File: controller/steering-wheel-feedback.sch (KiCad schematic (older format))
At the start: 5 parts

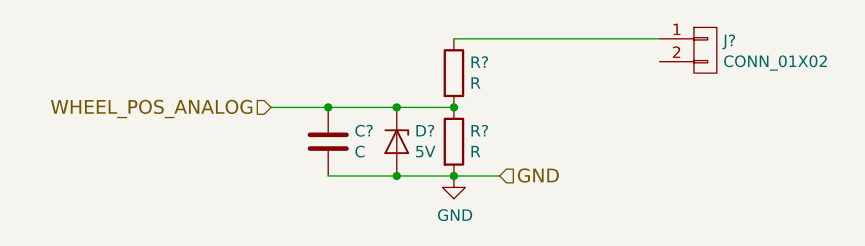
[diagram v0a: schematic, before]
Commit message: Add more stuff to controller, start sourcing parts
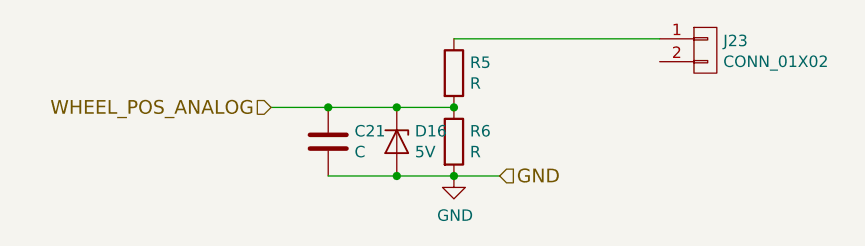
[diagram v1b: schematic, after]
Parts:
- gave numbers to parts that had none: 5
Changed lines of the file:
@@
 LIBS:mic-parts
 LIBS:controller-cache
-LIBS:line-interface-cache
 EELAYER 26 0
 EELAYER END
 $Descr A4 11693 8268
 encoding utf-8
-Sheet 6 6
+Sheet 5 10
 Title ""
 Date ""
@@
 $EndDescr
 $Comp
-L CONN_01X02 J?
+L CONN_01X02 J23
 U 1 1 58C0E3DC
 P 6150 3200
-F 0 "J?" H 6228 3241 50  0000 L CNN
+F 0 "J23" H 6228 3241 50  0000 L CNN
 F 1 "CONN_01X02" H 6228 3150 50  0000 L CNN
 F 2 "" H -3300 -450 50  0001 C CNN
@@
 	5950 3150 5050 3150
 $Comp
-L R R?
+L R R5
 U 1 1 58C0E434
 P 5050 3300
-F 0 "R?" H 5120 3346 50  0000 L CNN
+F 0 "R5" H 5120 3346 50  0000 L CNN
 F 1 "R" H 5120 3255 50  0000 L CNN
 F 2 "" V -2970 350 50  0001 C CNN
@@
 $EndComp
 $Comp
-L R R?
+L R R6
 U 1 1 58C0E45C
 P 5050 3600
-F 0 "R?" H 5120 3646 50  0000 L CNN
+F 0 "R6" H 5120 3646 50  0000 L CNN
 F 1 "R" H 5120 3555 50  0000 L CNN
 F 2 "" V -2970 650 50  0001 C CNN
@@
 $EndComp
 $Comp
-L GND #PWR?
+L GND #PWR07
 U 1 1 58C0E4A6
 P 5050 3750
-F 0 "#PWR?" H 5100 3800 50  0001 C CNN
+F 0 "#PWR07" H 5100 3800 50  0001 C CNN
 F 1 "GND" H 5055 3577 50  0000 C CNN
 F 2 "" H -3000 100 50  0001 C CNN
@@
 	4250 3450 5050 3450
 $Comp
-L D_Zener D?
+L D_Zener D16
 U 1 1 58C0E5E3
 P 4800 3600
-F 0 "D?" V 4754 3679 50  0000 L CNN
+F 0 "D16" V 4754 3679 50  0000 L CNN
 F 1 "5V" V 4845 3679 50  0000 L CNN
 F 2 "" H -2700 150 50  0001 C CNN
@@
 Connection ~ 4800 3450
 $Comp
-L C C?
+L C C21
 U 1 1 58C0E685
 P 4500 3600
-F 0 "C?" H 4615 3646 50  0000 L CNN
+F 0 "C21" H 4615 3646 50  0000 L CNN
 F 1 "C" H 4615 3555 50  0000 L CNN
 F 2 "" H -2962 50  50  0001 C CNN

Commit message: Change gas pedal interface so that it supports going up and down from the middle voltage so that it's compatible with Linde forklift gas mechanism
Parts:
- C21: footprint (none) -> Capacitors_SMD:C_0603_HandSoldering
- R5, R6: footprint (none) -> Resistors_SMD:R_0603_HandSoldering
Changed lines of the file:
@@
 F 0 "R5" H 5120 3346 50  0000 L CNN
 F 1 "R" H 5120 3255 50  0000 L CNN
-F 2 "" V -2970 350 50  0001 C CNN
+F 2 "Resistors_SMD:R_0603_HandSoldering" V -2970 350 50  0001 C CNN
 F 3 "" H -2900 350 50  0001 C CNN
 	1    5050 3300
@@
 F 0 "R6" H 5120 3646 50  0000 L CNN
 F 1 "R" H 5120 3555 50  0000 L CNN
-F 2 "" V -2970 650 50  0001 C CNN
+F 2 "Resistors_SMD:R_0603_HandSoldering" V -2970 650 50  0001 C CNN
 F 3 "" H -2900 650 50  0001 C CNN
 	1    5050 3600
@@
 $EndComp
 $Comp
-L GND #PWR07
+L GND #PWR7
 U 1 1 58C0E4A6
 P 5050 3750
-F 0 "#PWR07" H 5100 3800 50  0001 C CNN
+F 0 "#PWR7" H 5100 3800 50  0001 C CNN
 F 1 "GND" H 5055 3577 50  0000 C CNN
 F 2 "" H -3000 100 50  0001 C CNN
@@
 F 0 "C21" H 4615 3646 50  0000 L CNN
 F 1 "C" H 4615 3555 50  0000 L CNN
-F 2 "" H -2962 50  50  0001 C CNN
+F 2 "Capacitors_SMD:C_0603_HandSoldering" H -2962 50  50  0001 C CNN
 F 3 "" H -3000 200 50  0001 C CNN
 	1    4500 3600

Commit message: More or less final controller board
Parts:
- D16: footprint (none) -> Diodes_SMD:SOD-123; Distributor (none) -> 2690025; Manufacturer (none) -> ?; PartNo (none) -> ?
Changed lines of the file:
@@
 LIBS:valves
 LIBS:mic-parts
+LIBS:shield_arduino
 LIBS:controller-cache
 EELAYER 26 0
@@
 $EndComp
 $Comp
-L GND #PWR7
+L GND #PWR013
 U 1 1 58C0E4A6
 P 5050 3750
-F 0 "#PWR7" H 5100 3800 50  0001 C CNN
+F 0 "#PWR013" H 5100 3800 50  0001 C CNN
 F 1 "GND" H 5055 3577 50  0000 C CNN
 F 2 "" H -3000 100 50  0001 C CNN
@@
 F 0 "D16" V 4754 3679 50  0000 L CNN
 F 1 "5V" V 4845 3679 50  0000 L CNN
-F 2 "" H -2700 150 50  0001 C CNN
+F 2 "Diodes_SMD:SOD-123" H -2700 150 50  0001 C CNN
 F 3 "" H -2700 150 50  0001 C CNN
+F 4 "?" H 4800 3600 60  0001 C CNN "PartNo"
+F 5 "?" H 4800 3600 60  0001 C CNN "Manufacturer"
+F 6 "2690025" H 4800 3600 60  0001 C CNN "Distributor"
 	1    4800 3600
 	0    1    1    0

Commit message: Finish the routing, add some significant fixes: *correct to-252 pin numbering * longer pads for relays * fix footprint of the optocouplers
Also finish the routing
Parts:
- J23: footprint (none) -> Connectors_Terminal_Blocks:TerminalBlock_Pheonix_MKDS1.5-2pol; Distributor (none) -> ?; Manufacturer (none) -> ?; PartNo (none) -> ?
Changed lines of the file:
@@
 F 0 "J23" H 6228 3241 50  0000 L CNN
 F 1 "CONN_01X02" H 6228 3150 50  0000 L CNN
-F 2 "" H -3300 -450 50  0001 C CNN
+F 2 "Connectors_Terminal_Blocks:TerminalBlock_Pheonix_MKDS1.5-2pol" H -3300 -450 50  0001 C CNN
 F 3 "" H -3300 -450 50  0001 C CNN
+F 4 "?" H 6150 3200 60  0001 C CNN "PartNo"
+F 5 "?" H 6150 3200 60  0001 C CNN "Manufacturer"
+F 6 "?" H 6150 3200 60  0001 C CNN "Distributor"
 	1    6150 3200
 	1    0    0    -1

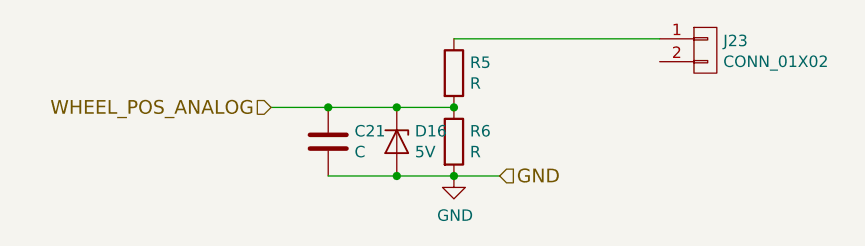
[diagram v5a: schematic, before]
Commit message: Update the 5 and 2 pin terminal footprints, shuffle around some tracks
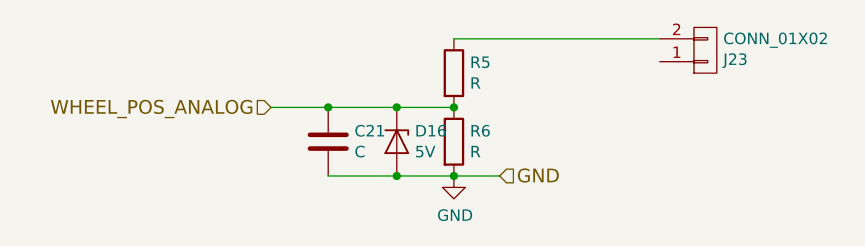
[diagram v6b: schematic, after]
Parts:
- J23: footprint Connectors_Terminal_Blocks:TerminalBlock_Pheonix_MKDS1.5-2pol -> smalsiukas-footpints:TerminalBlock_5.08-2pol
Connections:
- net at J23.1 (P1): no longer R5.1
- net at J23.2 (P2): now also R5.1
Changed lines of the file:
@@
 F 0 "J23" H 6228 3241 50  0000 L CNN
 F 1 "CONN_01X02" H 6228 3150 50  0000 L CNN
-F 2 "Connectors_Terminal_Blocks:TerminalBlock_Pheonix_MKDS1.5-2pol" H -3300 -450 50  0001 C CNN
+F 2 "smalsiukas-footpints:TerminalBlock_5.08-2pol" H -3300 -450 50  0001 C CNN
 F 3 "" H -3300 -450 50  0001 C CNN
 F 4 "?" H 6150 3200 60  0001 C CNN "PartNo"
@@
 F 6 "?" H 6150 3200 60  0001 C CNN "Distributor"
 	1    6150 3200
-	1    0    0    -1
+	1    0    0    1
 $EndComp
 Wire Wire Line

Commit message: send controller and line interface boards for manufacturing
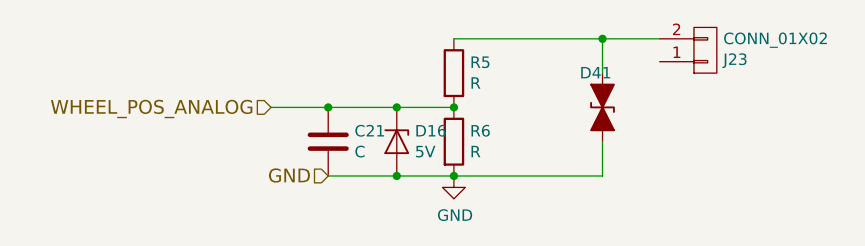
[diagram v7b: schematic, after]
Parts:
- added D41: D_TVS_ALT, Diodes_SMD:SOD-323, symbol D_TVS_ALT
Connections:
- net GND: now also D41.2 (A2)
- net at J23.2 (P2), R5.1: now also D41.1 (A1)
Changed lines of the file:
@@
 $EndComp
 Wire Wire Line
-	5950 3150 5050 3150
+	5050 3150 5950 3150
 $Comp
 L R R5
@@
 $EndComp
 $Comp
-L GND #PWR015
+L GND #PWR18
 U 1 1 58C0E4A6
 P 5050 3750
-F 0 "#PWR015" H 5100 3800 50  0001 C CNN
+F 0 "#PWR18" H 5100 3800 50  0001 C CNN
 F 1 "GND" H 5055 3577 50  0000 C CNN
 F 2 "" H -3000 100 50  0001 C CNN
@@
 $EndComp
 Wire Wire Line
-	4500 3750 5250 3750
+	4500 3750 5700 3750
 Connection ~ 5050 3750
 Connection ~ 5050 3450
@@
 Text HLabel 4250 3450 0    60   Input ~ 0
 WHEEL_POS_ANALOG
-Text HLabel 5250 3750 2    60   Input ~ 0
+Text HLabel 4500 3750 0    60   Input ~ 0
 GND
+$Comp
+L D_TVS_ALT D41
+U 1 1 58D0DEF8
+P 5700 3450
+F 0 "D41" V 5550 3350 50  0000 L CNN
+F 1 "D_TVS_ALT" V 5745 3529 50  0001 L CNN
+F 2 "Diodes_SMD:SOD-323" H 5700 3450 50  0001 C CNN
+F 3 "" H 5700 3450 50  0001 C CNN
+F 4 "?" H 5700 3450 60  0001 C CNN "PartNo"
+F 5 "?" H 5700 3450 60  0001 C CNN "Manufacturer"
+F 6 "2059012" H 5700 3450 60  0001 C CNN "Distributor"
+	1    5700 3450
+	0    1    1    0
+$EndComp
+Wire Wire Line
+	5700 3300 5700 3150
+Connection ~ 5700 3150
+Wire Wire Line
+	5700 3750 5700 3600
 $EndSCHEMATC
